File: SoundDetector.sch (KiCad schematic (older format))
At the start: 2 parts, among them J1 feather long, J2 feather short

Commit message: Draw schematic.
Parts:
- added J?: sound detector, symbol Connector_Generic:Conn_01x05
- added R? (x3): 1.74K, symbol Device:R_US
- added R? (x3): 3.3K, symbol Device:R_US
- added RV?: 10K, symbol Device:R_POT_US
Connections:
- net +3V3: now also RV?.3
- net A0: now also R?.1, R?.2
- net A1: now also R?.1, R?.2
- net A2: now also RV?.2
- net F0: now also R?.1, R?.2
- net GND: now also J?.1 (Pin_1), R?.2, R?.2, R?.2, RV?.1
- new net +5V: J?.2 (Pin_2)
- new net AUD: J?.5 (Pin_5), R?.1
- new net ENV: J?.4 (Pin_4), R?.1
- new net GATE: J?.3 (Pin_3), R?.1

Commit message: Use VUSB instead of +5V.
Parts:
- J3: renamed from J?; Description (none) -> CONN HDR 5POS 0.1 GOLD PCB; Digi-Key_PN (none) -> S7038-ND; MPN (none) -> PPPC051LFBN-RC
- gave numbers to parts that had none: 7
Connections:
- net +5V is gone; now on net VUSB: J3.2 (Pin_2)
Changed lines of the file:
@@
 	8350 2550 10500 2550
 $Comp
-L Connector_Generic:Conn_01x05 J?
+L Connector_Generic:Conn_01x05 J3
 U 1 1 5D38837E
 P 5500 3600
-F 0 "J?" H 5419 3175 50  0000 C CNN
+F 0 "J3" H 5419 3175 50  0000 C CNN
 F 1 "sound detector" H 5419 3266 50  0000 C CNN
 F 2 "" H 5500 3600 50  0001 C CNN
 F 3 "~" H 5500 3600 50  0001 C CNN
+F 4 "PPPC051LFBN-RC" H 5500 3600 50  0001 C CNN "MPN"
+F 5 "CONN HDR 5POS 0.1 GOLD PCB" H 5500 3600 50  0001 C CNN "Description"
+F 6 "S7038-ND" H 5500 3600 50  0001 C CNN "Digi-Key_PN"
 	1    5500 3600
 	1    0    0    1
@@
 GATE
 $Comp
-L power:GND #PWR?
+L power:GND #PWR04
 U 1 1 5D38939D
 P 5150 3900
-F 0 "#PWR?" H 5150 3650 50  0001 C CNN
+F 0 "#PWR04" H 5150 3650 50  0001 C CNN
 F 1 "GND" H 5155 3727 50  0000 C CNN
 F 2 "" H 5150 3900 50  0001 C CNN
@@
 	5300 3600 5100 3600
 $Comp
-L power:+5V #PWR?
-U 1 1 5D38AF28
-P 4900 3550
-F 0 "#PWR?" H 4900 3400 50  0001 C CNN
-F 1 "+5V" H 4915 3723 50  0000 C CNN
-F 2 "" H 4900 3550 50  0001 C CNN
-F 3 "" H 4900 3550 50  0001 C CNN
-	1    4900 3550
-	1    0    0    -1
-$EndComp
-Wire Wire Line
-	5300 3700 4900 3700
-Wire Wire Line
-	4900 3700 4900 3550
-$Comp
-L Device:R_US R?
+L Device:R_US R1
 U 1 1 5D38B8FD
 P 6650 3350
-F 0 "R?" H 6718 3396 50  0000 L CNN
+F 0 "R1" H 6718 3396 50  0000 L CNN
 F 1 "1.74K" H 6718 3305 50  0000 L CNN
 F 2 "" V 6690 3340 50  0001 C CNN
@@
 $EndComp
 $Comp
-L Device:R_US R?
+L Device:R_US R2
 U 1 1 5D38B935
 P 6650 3850
-F 0 "R?" H 6718 3896 50  0000 L CNN
+F 0 "R2" H 6718 3896 50  0000 L CNN
 F 1 "3.3K" H 6718 3805 50  0000 L CNN
 F 2 "" V 6690 3840 50  0001 C CNN
@@
 	6650 3700 6650 3600
 $Comp
-L power:GND #PWR?
+L power:GND #PWR05
 U 1 1 5D38C445
 P 6650 4100
-F 0 "#PWR?" H 6650 3850 50  0001 C CNN
+F 0 "#PWR05" H 6650 3850 50  0001 C CNN
 F 1 "GND" H 6655 3927 50  0000 C CNN
 F 2 "" H 6650 4100 50  0001 C CNN
@@
 	6650 3200 6650 3000
 $Comp
-L Device:R_US R?
+L Device:R_US R3
 U 1 1 5D38E30B
 P 7350 3350
-F 0 "R?" H 7418 3396 50  0000 L CNN
+F 0 "R3" H 7418 3396 50  0000 L CNN
 F 1 "1.74K" H 7418 3305 50  0000 L CNN
 F 2 "" V 7390 3340 50  0001 C CNN
@@
 $EndComp
 $Comp
-L Device:R_US R?
+L Device:R_US R4
 U 1 1 5D38E314
 P 7350 3850
-F 0 "R?" H 7418 3896 50  0000 L CNN
+F 0 "R4" H 7418 3896 50  0000 L CNN
 F 1 "3.3K" H 7418 3805 50  0000 L CNN
 F 2 "" V 7390 3840 50  0001 C CNN
@@
 	7350 3700 7350 3600
 $Comp
-L power:GND #PWR?
+L power:GND #PWR06
 U 1 1 5D38E31B
 P 7350 4100
-F 0 "#PWR?" H 7350 3850 50  0001 C CNN
+F 0 "#PWR06" H 7350 3850 50  0001 C CNN
 F 1 "GND" H 7355 3927 50  0000 C CNN
 F 2 "" H 7350 4100 50  0001 C CNN
@@
 	7350 3200 7350 3000
 $Comp
-L Device:R_US R?
+L Device:R_US R5
 U 1 1 5D38FB9F
 P 8100 3350
-F 0 "R?" H 8168 3396 50  0000 L CNN
+F 0 "R5" H 8168 3396 50  0000 L CNN
 F 1 "1.74K" H 8168 3305 50  0000 L CNN
 F 2 "" V 8140 3340 50  0001 C CNN
@@
 $EndComp
 $Comp
-L Device:R_US R?
+L Device:R_US R6
 U 1 1 5D38FBA8
 P 8100 3850
-F 0 "R?" H 8168 3896 50  0000 L CNN
+F 0 "R6" H 8168 3896 50  0000 L CNN
 F 1 "3.3K" H 8168 3805 50  0000 L CNN
 F 2 "" V 8140 3840 50  0001 C CNN
@@
 	8100 3700 8100 3600
 $Comp
-L power:GND #PWR?
+L power:GND #PWR07
 U 1 1 5D38FBAF
 P 8100 4100
-F 0 "#PWR?" H 8100 3850 50  0001 C CNN
+F 0 "#PWR07" H 8100 3850 50  0001 C CNN
 F 1 "GND" H 8105 3927 50  0000 C CNN
 F 2 "" H 8100 4100 50  0001 C CNN
@@
 	8100 3200 8100 3000
 $Comp
-L Device:R_POT_US RV?
+L Device:R_POT_US RV1
 U 1 1 5D390E6C
 P 9150 3300
-F 0 "RV?" H 9082 3346 50  0000 R CNN
+F 0 "RV1" H 9082 3346 50  0000 R CNN
 F 1 "10K" H 9082 3255 50  0000 R CNN
 F 2 "" H 9150 3300 50  0001 C CNN
@@
 $EndComp
 $Comp
-L power:GND #PWR?
+L power:GND #PWR09
 U 1 1 5D38AF85
 P 9150 3550
-F 0 "#PWR?" H 9150 3300 50  0001 C CNN
+F 0 "#PWR09" H 9150 3300 50  0001 C CNN
 F 1 "GND" H 9155 3377 50  0000 C CNN
 F 2 "" H 9150 3550 50  0001 C CNN
@@
 $EndComp
 $Comp
-L power:+3.3V #PWR?
+L power:+3.3V #PWR08
 U 1 1 5D38AFDA
 P 9150 3050
-F 0 "#PWR?" H 9150 2900 50  0001 C CNN
+F 0 "#PWR08" H 9150 2900 50  0001 C CNN
 F 1 "+3.3V" H 9165 3223 50  0000 C CNN
 F 2 "" H 9150 3050 50  0001 C CNN
@@
 Wire Wire Line
 	9300 3300 9500 3300
+Text Label 5100 3700 0    50   ~ 0
+VUSB
+Wire Wire Line
+	5100 3700 5300 3700
 $EndSCHEMATC

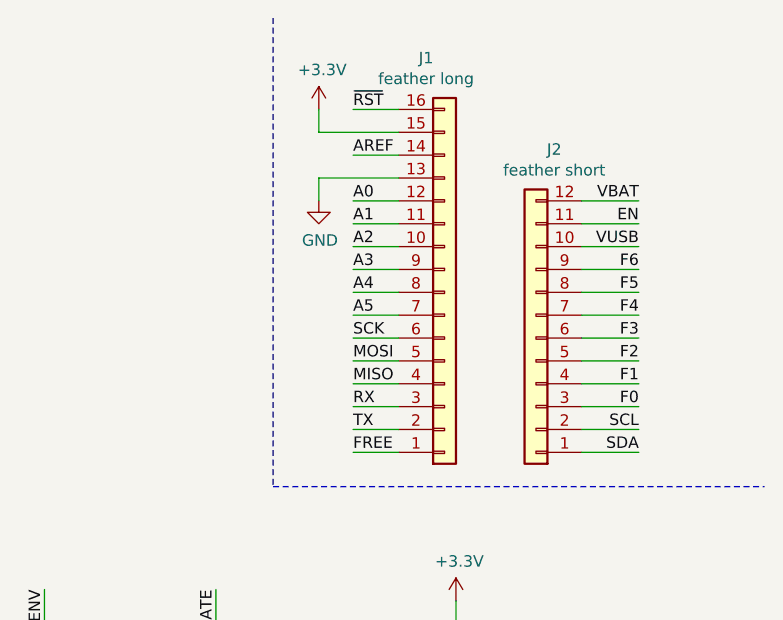
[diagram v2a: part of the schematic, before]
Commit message: Got it passing ERC.
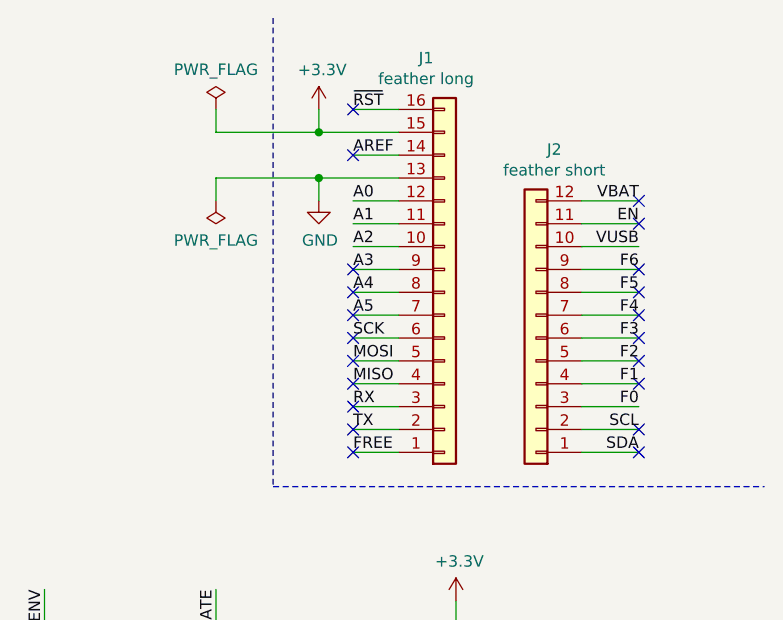
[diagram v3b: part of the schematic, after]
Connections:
- no-connect marks 0 -> 21
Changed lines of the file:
@@
 Wire Wire Line
 	5100 3700 5300 3700
+$Comp
+L power:PWR_FLAG #FLG0101
+U 1 1 5D390689
+P 8100 900
+F 0 "#FLG0101" H 8100 975 50  0001 C CNN
+F 1 "PWR_FLAG" H 8100 1074 50  0000 C CNN
+F 2 "" H 8100 900 50  0001 C CNN
+F 3 "~" H 8100 900 50  0001 C CNN
+	1    8100 900
+	1    0    0    -1
+$EndComp
+$Comp
+L power:PWR_FLAG #FLG0102
+U 1 1 5D3906C9
+P 8100 1300
+F 0 "#FLG0102" H 8100 1375 50  0001 C CNN
+F 1 "PWR_FLAG" H 8100 1473 50  0000 C CNN
+F 2 "" H 8100 1300 50  0001 C CNN
+F 3 "~" H 8100 1300 50  0001 C CNN
+	1    8100 1300
+	1    0    0    1
+$EndComp
+Wire Wire Line
+	8100 900  8100 1000
+Wire Wire Line
+	8100 1000 8550 1000
+Connection ~ 8550 1000
+Wire Wire Line
+	8100 1300 8100 1200
+Wire Wire Line
+	8100 1200 8550 1200
+Connection ~ 8550 1200
+NoConn ~ 8700 1100
+NoConn ~ 8700 1600
+NoConn ~ 8700 1700
+NoConn ~ 8700 1800
+NoConn ~ 8700 1900
+NoConn ~ 8700 2000
+NoConn ~ 8700 2100
+NoConn ~ 8700 2200
+NoConn ~ 8700 2300
+NoConn ~ 8700 2400
+NoConn ~ 9950 1300
+NoConn ~ 9950 1400
+NoConn ~ 9950 1600
+NoConn ~ 9950 1700
+NoConn ~ 9950 1800
+NoConn ~ 9950 1900
+NoConn ~ 9950 2000
+NoConn ~ 9950 2100
+NoConn ~ 9950 2300
+NoConn ~ 9950 2400
+NoConn ~ 8700 900
 $EndSCHEMATC

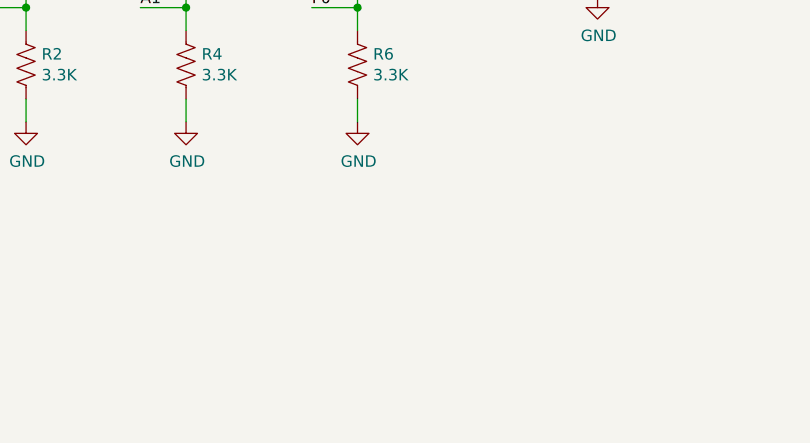
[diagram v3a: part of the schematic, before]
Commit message: Add a couple decouplng capacitors, in case they are needed.
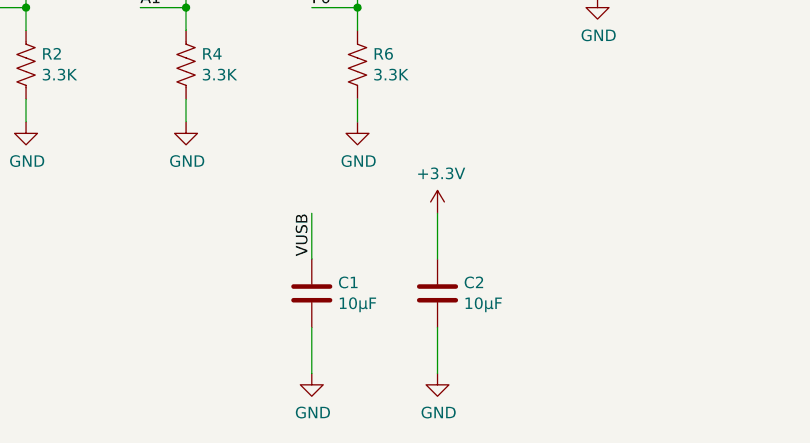
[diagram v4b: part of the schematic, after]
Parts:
- added C1, C2: 10μF, symbol Device:C
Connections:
- net +3V3: now also C2.1
- net GND: now also C1.2, C2.2
- net VUSB: now also C1.1
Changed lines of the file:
@@
 NoConn ~ 9950 2400
 NoConn ~ 8700 900
+$Comp
+L Device:C C1
+U 1 1 5D3A7CD1
+P 7900 4850
+F 0 "C1" H 8015 4896 50  0000 L CNN
+F 1 "10μF" H 8015 4805 50  0000 L CNN
+F 2 "" H 7938 4700 50  0001 C CNN
+F 3 "~" H 7900 4850 50  0001 C CNN
+F 4 "C0805C106K8PACTU" H 7900 4850 50  0001 C CNN "MPN"
+F 5 "CAP CER 10UF 10V X5R 0805" H 7900 4850 50  0001 C CNN "Description"
+F 6 "399-4925-1-ND" H 7900 4850 50  0001 C CNN "Digi-Key_PN"
+	1    7900 4850
+	1    0    0    -1
+$EndComp
+Text Label 7900 4500 3    50   ~ 0
+VUSB
+$Comp
+L power:GND #PWR03
+U 1 1 5D3A7D3E
+P 7900 5200
+F 0 "#PWR03" H 7900 4950 50  0001 C CNN
+F 1 "GND" H 7905 5027 50  0000 C CNN
+F 2 "" H 7900 5200 50  0001 C CNN
+F 3 "" H 7900 5200 50  0001 C CNN
+	1    7900 5200
+	1    0    0    -1
+$EndComp
+Wire Wire Line
+	7900 4500 7900 4700
+Wire Wire Line
+	7900 5200 7900 5000
+$Comp
+L Device:C C2
+U 1 1 5D38CF09
+P 8450 4850
+F 0 "C2" H 8565 4896 50  0000 L CNN
+F 1 "10μF" H 8565 4805 50  0000 L CNN
+F 2 "" H 8488 4700 50  0001 C CNN
+F 3 "~" H 8450 4850 50  0001 C CNN
+F 4 "C0805C106K8PACTU" H 8450 4850 50  0001 C CNN "MPN"
+F 5 "CAP CER 10UF 10V X5R 0805" H 8450 4850 50  0001 C CNN "Description"
+F 6 "399-4925-1-ND" H 8450 4850 50  0001 C CNN "Digi-Key_PN"
+	1    8450 4850
+	1    0    0    -1
+$EndComp
+$Comp
+L power:GND #PWR011
+U 1 1 5D38CF10
+P 8450 5200
+F 0 "#PWR011" H 8450 4950 50  0001 C CNN
+F 1 "GND" H 8455 5027 50  0000 C CNN
+F 2 "" H 8450 5200 50  0001 C CNN
+F 3 "" H 8450 5200 50  0001 C CNN
+	1    8450 5200
+	1    0    0    -1
+$EndComp
+Wire Wire Line
+	8450 4500 8450 4700
+Wire Wire Line
+	8450 5200 8450 5000
+$Comp
+L power:+3.3V #PWR010
+U 1 1 5D38E039
+P 8450 4500
+F 0 "#PWR010" H 8450 4350 50  0001 C CNN
+F 1 "+3.3V" H 8465 4673 50  0000 C CNN
+F 2 "" H 8450 4500 50  0001 C CNN
+F 3 "" H 8450 4500 50  0001 C CNN
+	1    8450 4500
+	1    0    0    -1
+$EndComp
 $EndSCHEMATC

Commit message: Assign footprints.
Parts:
- C1, C2: footprint (none) -> Capacitor_SMD:C_0805_2012Metric_Pad1.15x1.40mm_HandSolder
- J3: footprint (none) -> Connector_PinSocket_2.54mm:PinSocket_1x05_P2.54mm_Vertical
- R1, R2, R3, R4, R5, R6: footprint (none) -> Resistor_THT:R_Axial_DIN0207_L6.3mm_D2.5mm_P7.62mm_Horizontal
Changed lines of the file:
@@
 F 0 "J3" H 5419 3175 50  0000 C CNN
 F 1 "sound detector" H 5419 3266 50  0000 C CNN
-F 2 "" H 5500 3600 50  0001 C CNN
+F 2 "Connector_PinSocket_2.54mm:PinSocket_1x05_P2.54mm_Vertical" H 5500 3600 50  0001 C CNN
 F 3 "~" H 5500 3600 50  0001 C CNN
 F 4 "PPPC051LFBN-RC" H 5500 3600 50  0001 C CNN "MPN"
@@
 F 0 "R1" H 6718 3396 50  0000 L CNN
 F 1 "1.74K" H 6718 3305 50  0000 L CNN
-F 2 "" V 6690 3340 50  0001 C CNN
+F 2 "Resistor_THT:R_Axial_DIN0207_L6.3mm_D2.5mm_P7.62mm_Horizontal" V 6690 3340 50  0001 C CNN
 F 3 "~" H 6650 3350 50  0001 C CNN
 F 4 "MFR-25FBF52-1K74" H 6650 3350 50  0001 C CNN "MPN"
@@
 F 0 "R2" H 6718 3896 50  0000 L CNN
 F 1 "3.3K" H 6718 3805 50  0000 L CNN
-F 2 "" V 6690 3840 50  0001 C CNN
+F 2 "Resistor_THT:R_Axial_DIN0207_L6.3mm_D2.5mm_P7.62mm_Horizontal" V 6690 3840 50  0001 C CNN
 F 3 "~" H 6650 3850 50  0001 C CNN
 F 4 "RNMF14FTC3K30" H 6650 3850 50  0001 C CNN "MPN"
@@
 F 0 "R3" H 7418 3396 50  0000 L CNN
 F 1 "1.74K" H 7418 3305 50  0000 L CNN
-F 2 "" V 7390 3340 50  0001 C CNN
+F 2 "Resistor_THT:R_Axial_DIN0207_L6.3mm_D2.5mm_P7.62mm_Horizontal" V 7390 3340 50  0001 C CNN
 F 3 "~" H 7350 3350 50  0001 C CNN
 F 4 "MFR-25FBF52-1K74" H 7350 3350 50  0001 C CNN "MPN"
@@
 F 0 "R4" H 7418 3896 50  0000 L CNN
 F 1 "3.3K" H 7418 3805 50  0000 L CNN
-F 2 "" V 7390 3840 50  0001 C CNN
+F 2 "Resistor_THT:R_Axial_DIN0207_L6.3mm_D2.5mm_P7.62mm_Horizontal" V 7390 3840 50  0001 C CNN
 F 3 "~" H 7350 3850 50  0001 C CNN
 F 4 "RNMF14FTC3K30" H 7350 3850 50  0001 C CNN "MPN"
@@
 F 0 "R5" H 8168 3396 50  0000 L CNN
 F 1 "1.74K" H 8168 3305 50  0000 L CNN
-F 2 "" V 8140 3340 50  0001 C CNN
+F 2 "Resistor_THT:R_Axial_DIN0207_L6.3mm_D2.5mm_P7.62mm_Horizontal" V 8140 3340 50  0001 C CNN
 F 3 "~" H 8100 3350 50  0001 C CNN
 F 4 "MFR-25FBF52-1K74" H 8100 3350 50  0001 C CNN "MPN"
@@
 F 0 "R6" H 8168 3896 50  0000 L CNN
 F 1 "3.3K" H 8168 3805 50  0000 L CNN
-F 2 "" V 8140 3840 50  0001 C CNN
+F 2 "Resistor_THT:R_Axial_DIN0207_L6.3mm_D2.5mm_P7.62mm_Horizontal" V 8140 3840 50  0001 C CNN
 F 3 "~" H 8100 3850 50  0001 C CNN
 F 4 "RNMF14FTC3K30" H 8100 3850 50  0001 C CNN "MPN"
@@
 F 0 "C1" H 8015 4896 50  0000 L CNN
 F 1 "10μF" H 8015 4805 50  0000 L CNN
-F 2 "" H 7938 4700 50  0001 C CNN
+F 2 "Capacitor_SMD:C_0805_2012Metric_Pad1.15x1.40mm_HandSolder" H 7938 4700 50  0001 C CNN
 F 3 "~" H 7900 4850 50  0001 C CNN
 F 4 "C0805C106K8PACTU" H 7900 4850 50  0001 C CNN "MPN"
@@
 F 0 "C2" H 8565 4896 50  0000 L CNN
 F 1 "10μF" H 8565 4805 50  0000 L CNN
-F 2 "" H 8488 4700 50  0001 C CNN
+F 2 "Capacitor_SMD:C_0805_2012Metric_Pad1.15x1.40mm_HandSolder" H 8488 4700 50  0001 C CNN
 F 3 "~" H 8450 4850 50  0001 C CNN
 F 4 "C0805C106K8PACTU" H 8450 4850 50  0001 C CNN "MPN"

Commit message: Assign potentiometer footprint.
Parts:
- RV1: footprint (none) -> footprints:Potentiometer_Bourns_3352T_Vertical
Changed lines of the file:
@@
 F 0 "RV1" H 9082 3346 50  0000 R CNN
 F 1 "10K" H 9082 3255 50  0000 R CNN
-F 2 "" H 9150 3300 50  0001 C CNN
+F 2 "footprints:Potentiometer_Bourns_3352T_Vertical" H 9150 3300 50  0001 C CNN
 F 3 "~" H 9150 3300 50  0001 C CNN
 F 4 "3352T-1-103LF" H 9150 3300 50  0001 C CNN "MPN"

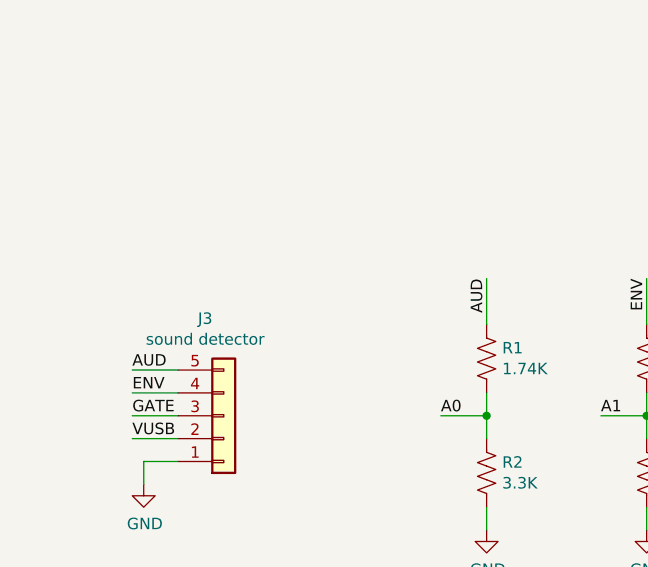
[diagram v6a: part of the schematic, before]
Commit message: Add metadata to schematic.
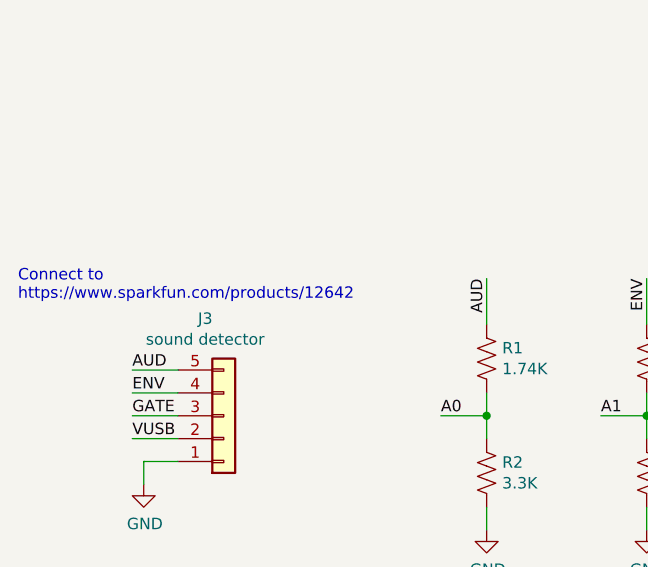
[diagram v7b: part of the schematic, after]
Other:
- note added: "Connect to\nhttps://www.sparkfun.com/products/12642"
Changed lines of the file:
@@
 encoding utf-8
 Sheet 1 1
-Title ""
-Date ""
-Rev ""
+Title "Sound Detector FeatherWing"
+Date "2019-07-24"
+Rev "1.0"
 Comp ""
 Comment1 ""
@@
 	1    0    0    -1
 $EndComp
+Text Notes 4600 3100 0    50   ~ 0
+Connect to\nhttps://www.sparkfun.com/products/12642
 $EndSCHEMATC
